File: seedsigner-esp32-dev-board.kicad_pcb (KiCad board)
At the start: 2 copper layers, 73.7 x 86.4 mm, 4 parts, among them J1 Conn_01x05, U1 ESP32-S2-SAOLA-1M, U2 OV_CAMERA, U3 RASPBERRY_PI_3_MODEL_B+

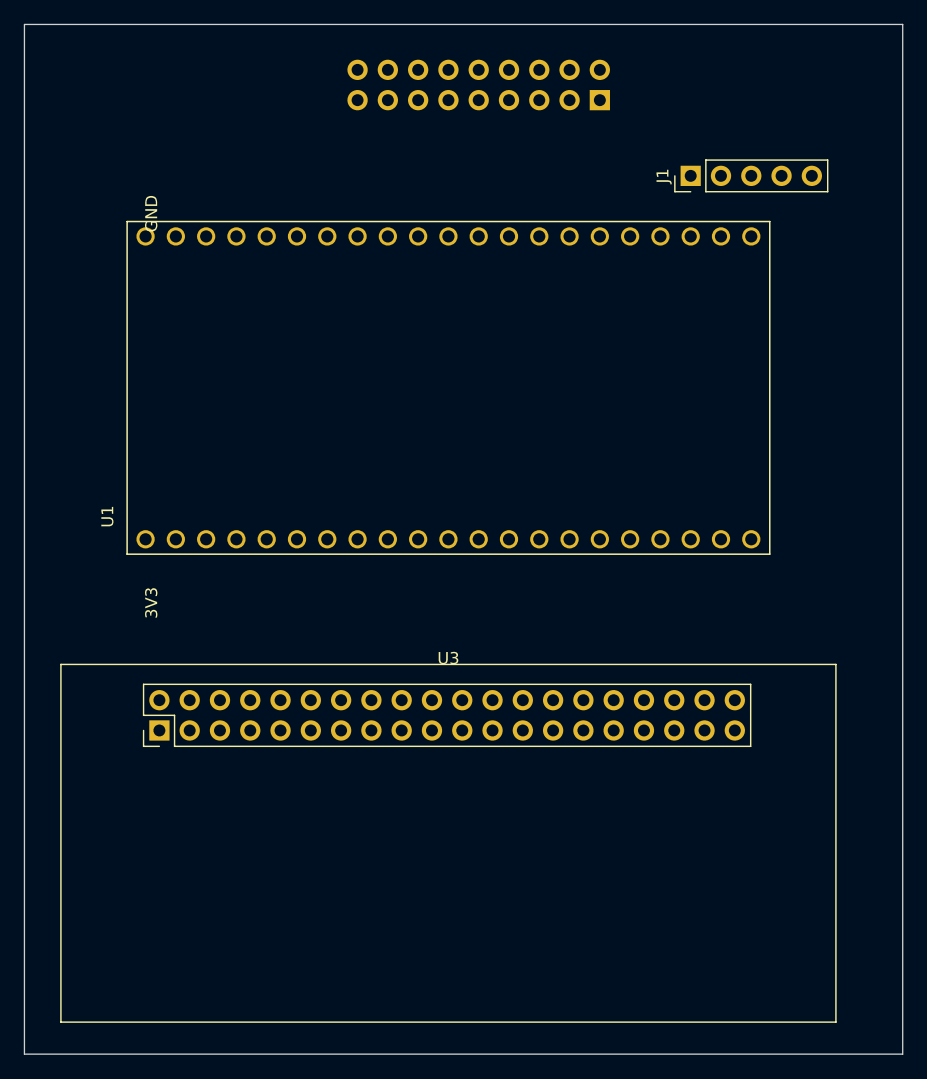
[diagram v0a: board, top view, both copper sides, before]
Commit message: add symbol libraries
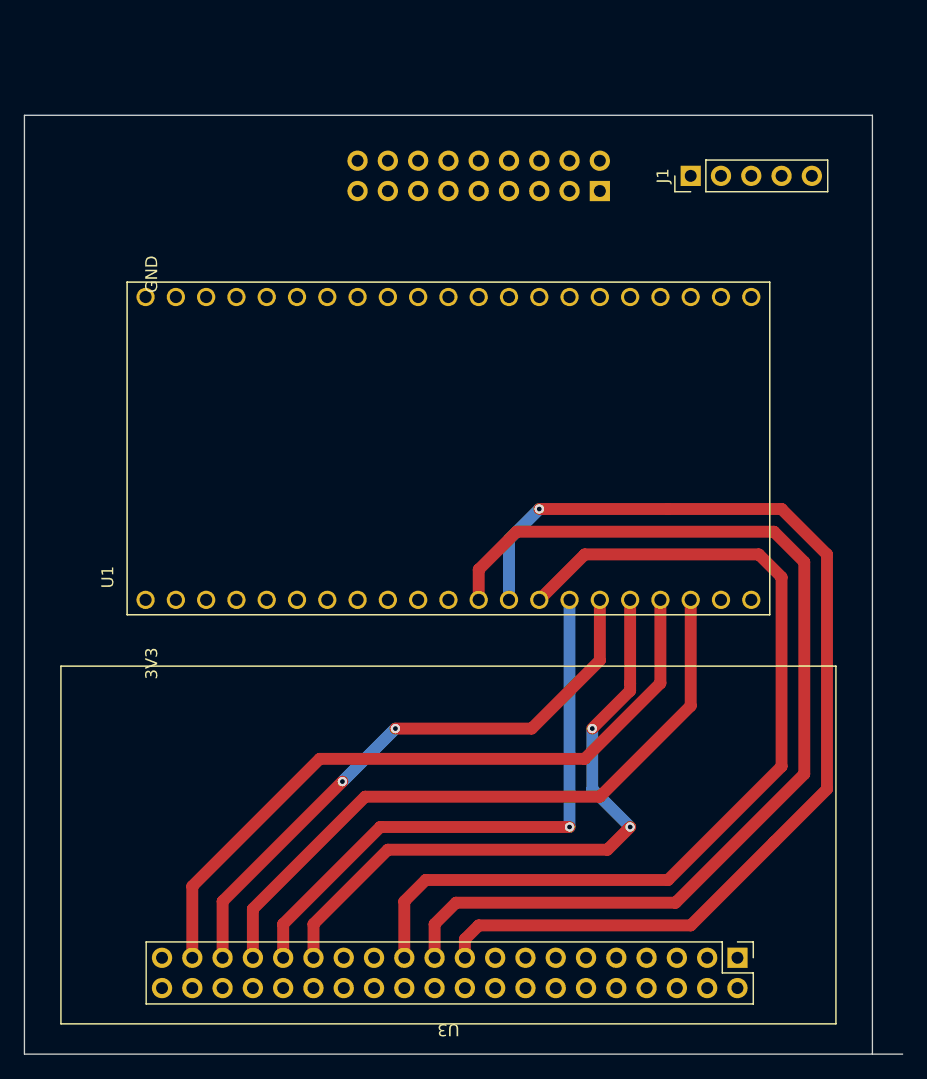
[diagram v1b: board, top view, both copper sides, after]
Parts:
- moved U3 30.1 mm to (162.6, 124.5), turned to 180 degrees
- moved U2 7.62 mm to (165.1, 53.3)
- moved U1 5.08 mm to (162.6, 76.2)
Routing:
- net /SPI_MOSI: track 0.00 -> 91.2 mm, vias 0 -> 1
- net /SPI_CS: track 0.00 -> 89.0 mm
- net /SPI_SCLK: track 0.00 -> 79.6 mm
- net /JOYSTICK_RIGHT: track 0.00 -> 59.3 mm
- net /JOYSTICK_PRESS: track 0.00 -> 56.8 mm
- net /JOYSTICK_LEFT: track 0.00 -> 54.4 mm, vias 0 -> 2
- net /JOYSTICK_DOWN: track 0.00 -> 49.8 mm, vias 0 -> 2
- net /JOYSTICK_UP: track 0.00 -> 49.3 mm, vias 0 -> 1
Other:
- board size 73.7 x 86.4 mm -> 73.7 x 78.7 mm

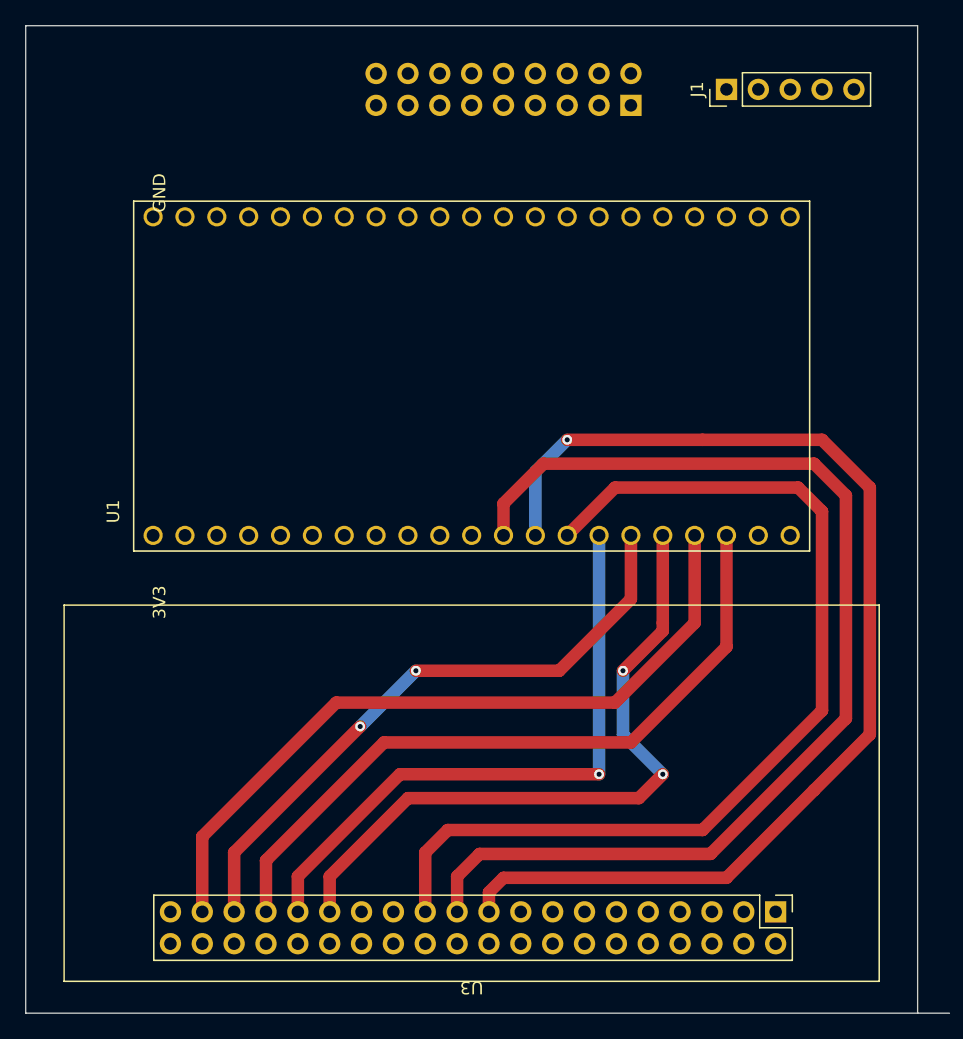
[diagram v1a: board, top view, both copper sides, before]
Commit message: update readme with links, add 3.3v to display and cap
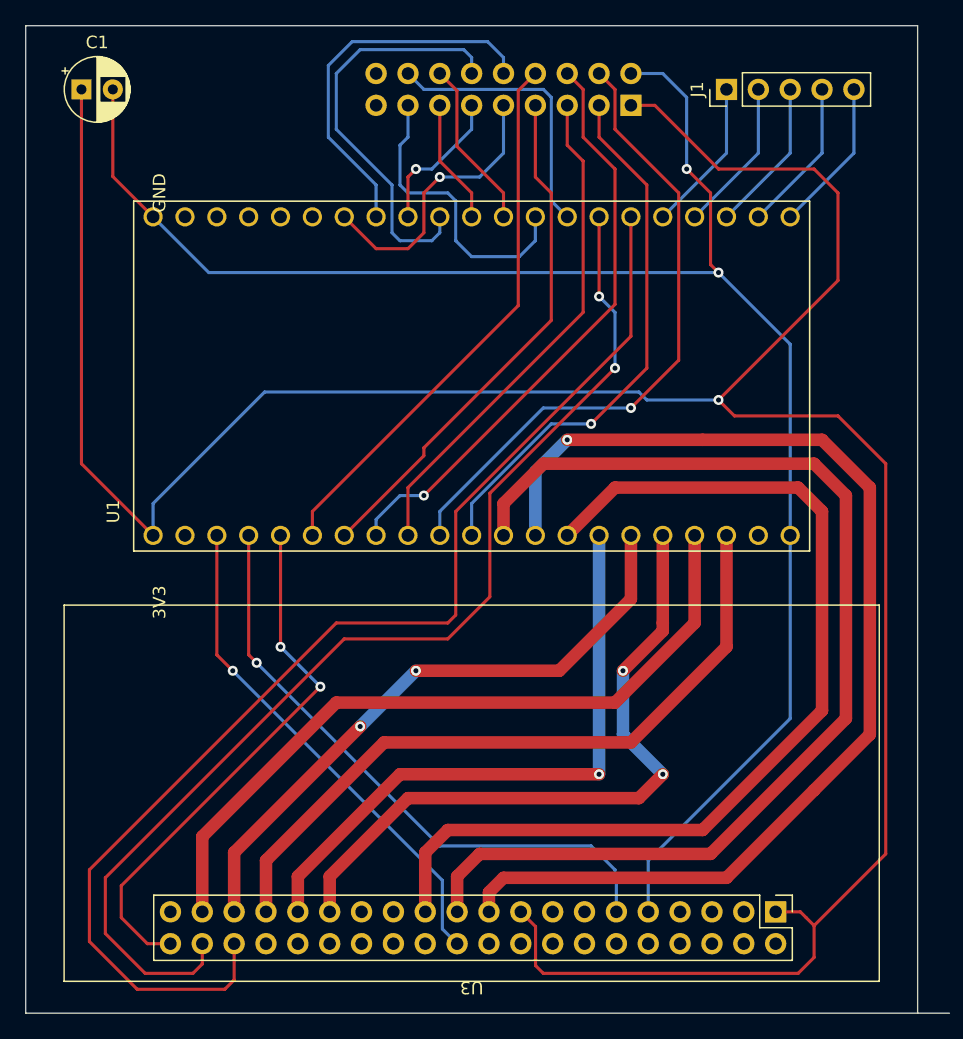
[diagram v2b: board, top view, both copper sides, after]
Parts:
- added C1: C_Polarized, Capacitor_THT:CP_Radial_D5.0mm_P2.50mm, F.Cu at (131.4, 53.3)
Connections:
- U3 pad 1: Net-(U3-Pad1) -> +3.3V
- U3 pad 17: Net-(U3-Pad1) -> +3.3V
- U3 pad 36: unconnected-(U3-Pad36) -> /KEY3
- U3 pad 38: unconnected-(U3-Pad38) -> /KEY2
- U3 pad 40: unconnected-(U3-Pad40) -> /KEY1
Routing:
- net +3.3V: track 0.00 -> 217.8 mm, vias 0 -> 1
- net GND: track 0.00 -> 136.7 mm, vias 0 -> 2
- net /KEY3: track 0.00 -> 97.2 mm
- net /KEY2: track 0.00 -> 90.3 mm, vias 0 -> 2
- net /SDA: track 0.00 -> 51.4 mm, vias 0 -> 1
- net /RST: track 0.00 -> 49.2 mm, vias 0 -> 1
- net /HREF: track 0.00 -> 47.4 mm, vias 0 -> 1
- net /XCLK: track 0.00 -> 44.2 mm
- net /SCL: track 0.00 -> 43.5 mm, vias 0 -> 1
- net /KEY1: track 0.00 -> 43.2 mm, vias 0 -> 2
- net /PCLK: track 0.00 -> 41.7 mm
- net /VSYNC: track 0.00 -> 40.6 mm
- net /DC: track 0.00 -> 40.5 mm, vias 0 -> 1
- net /D6: track 0.00 -> 33.3 mm
- net /D8: track 0.00 -> 30.2 mm
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
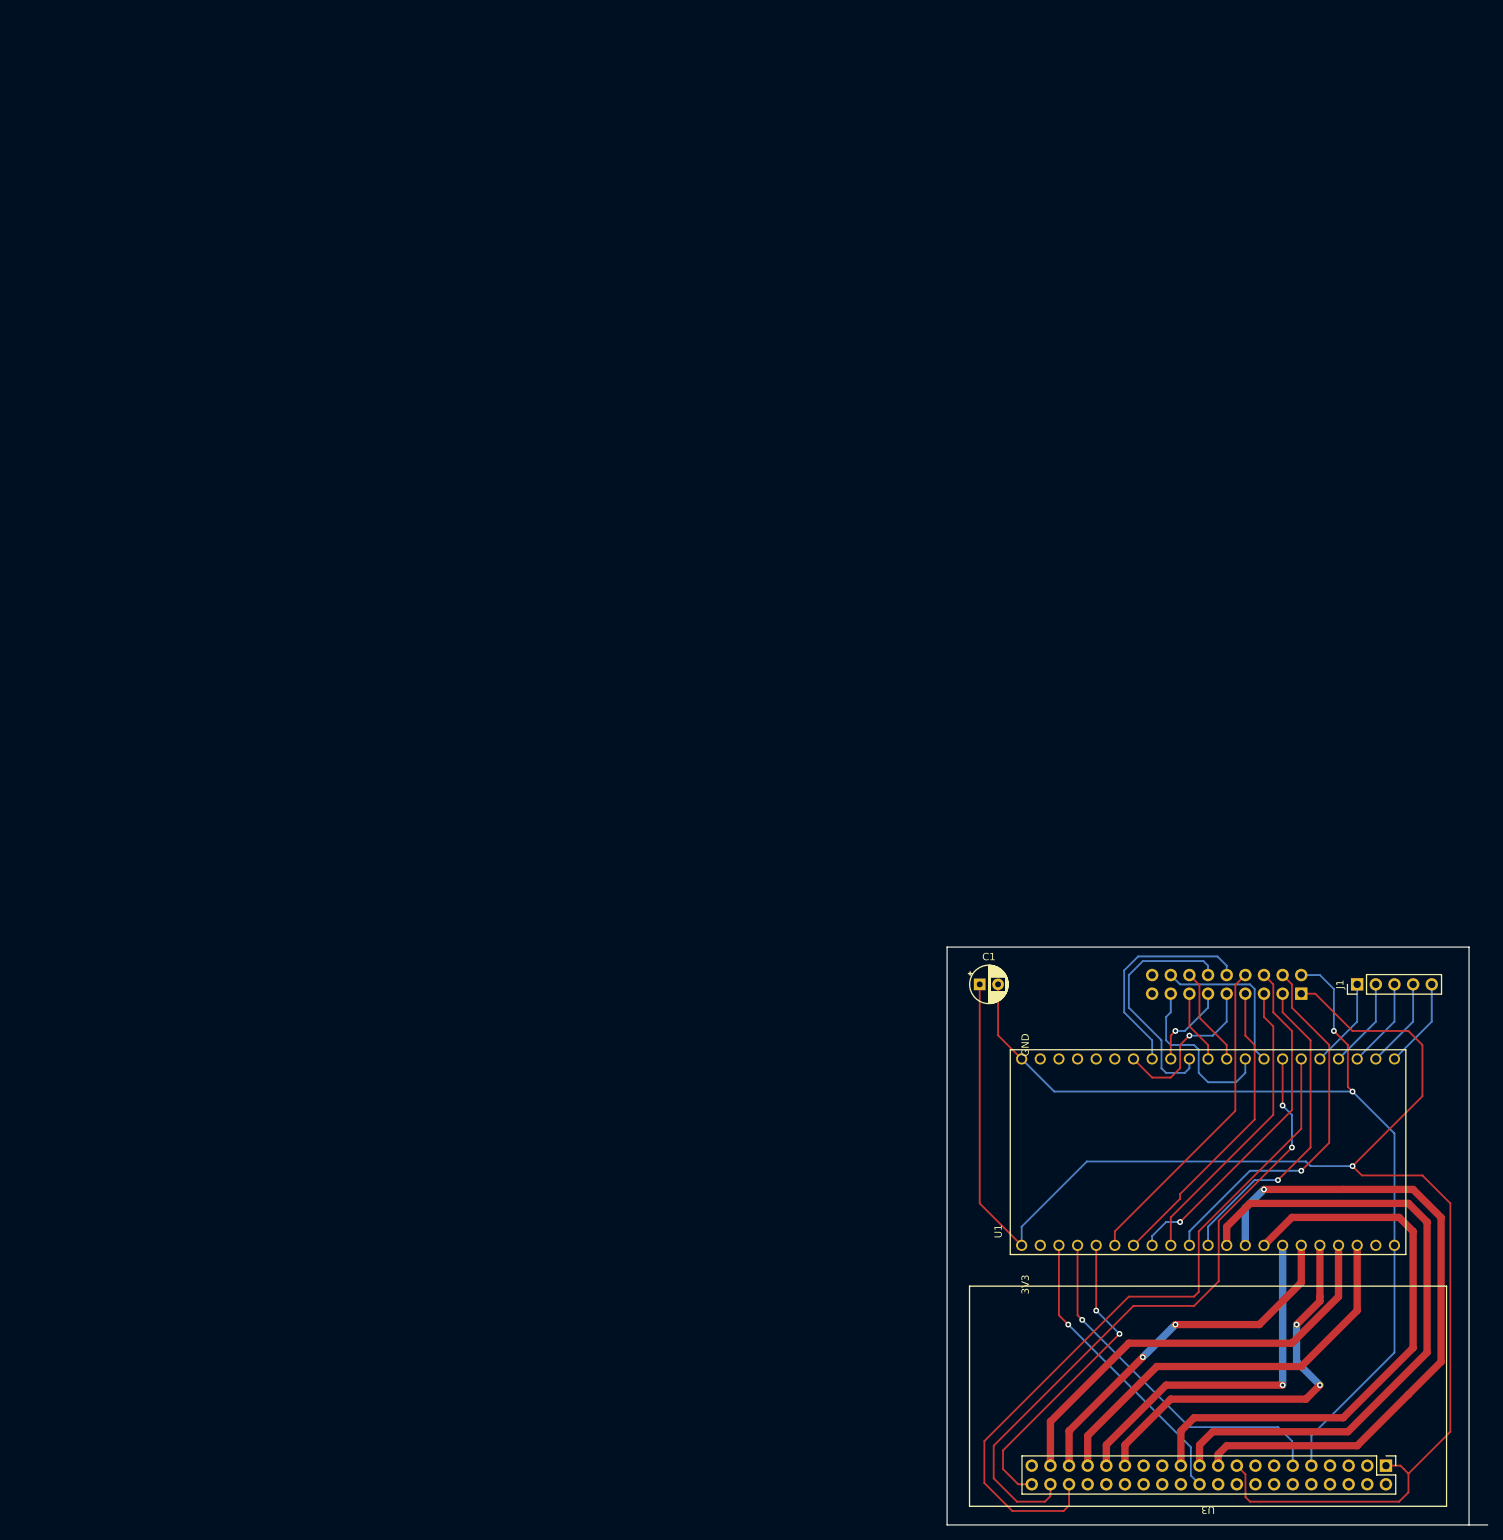
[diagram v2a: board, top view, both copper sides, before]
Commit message: rewire all the pins to make routing cleaner
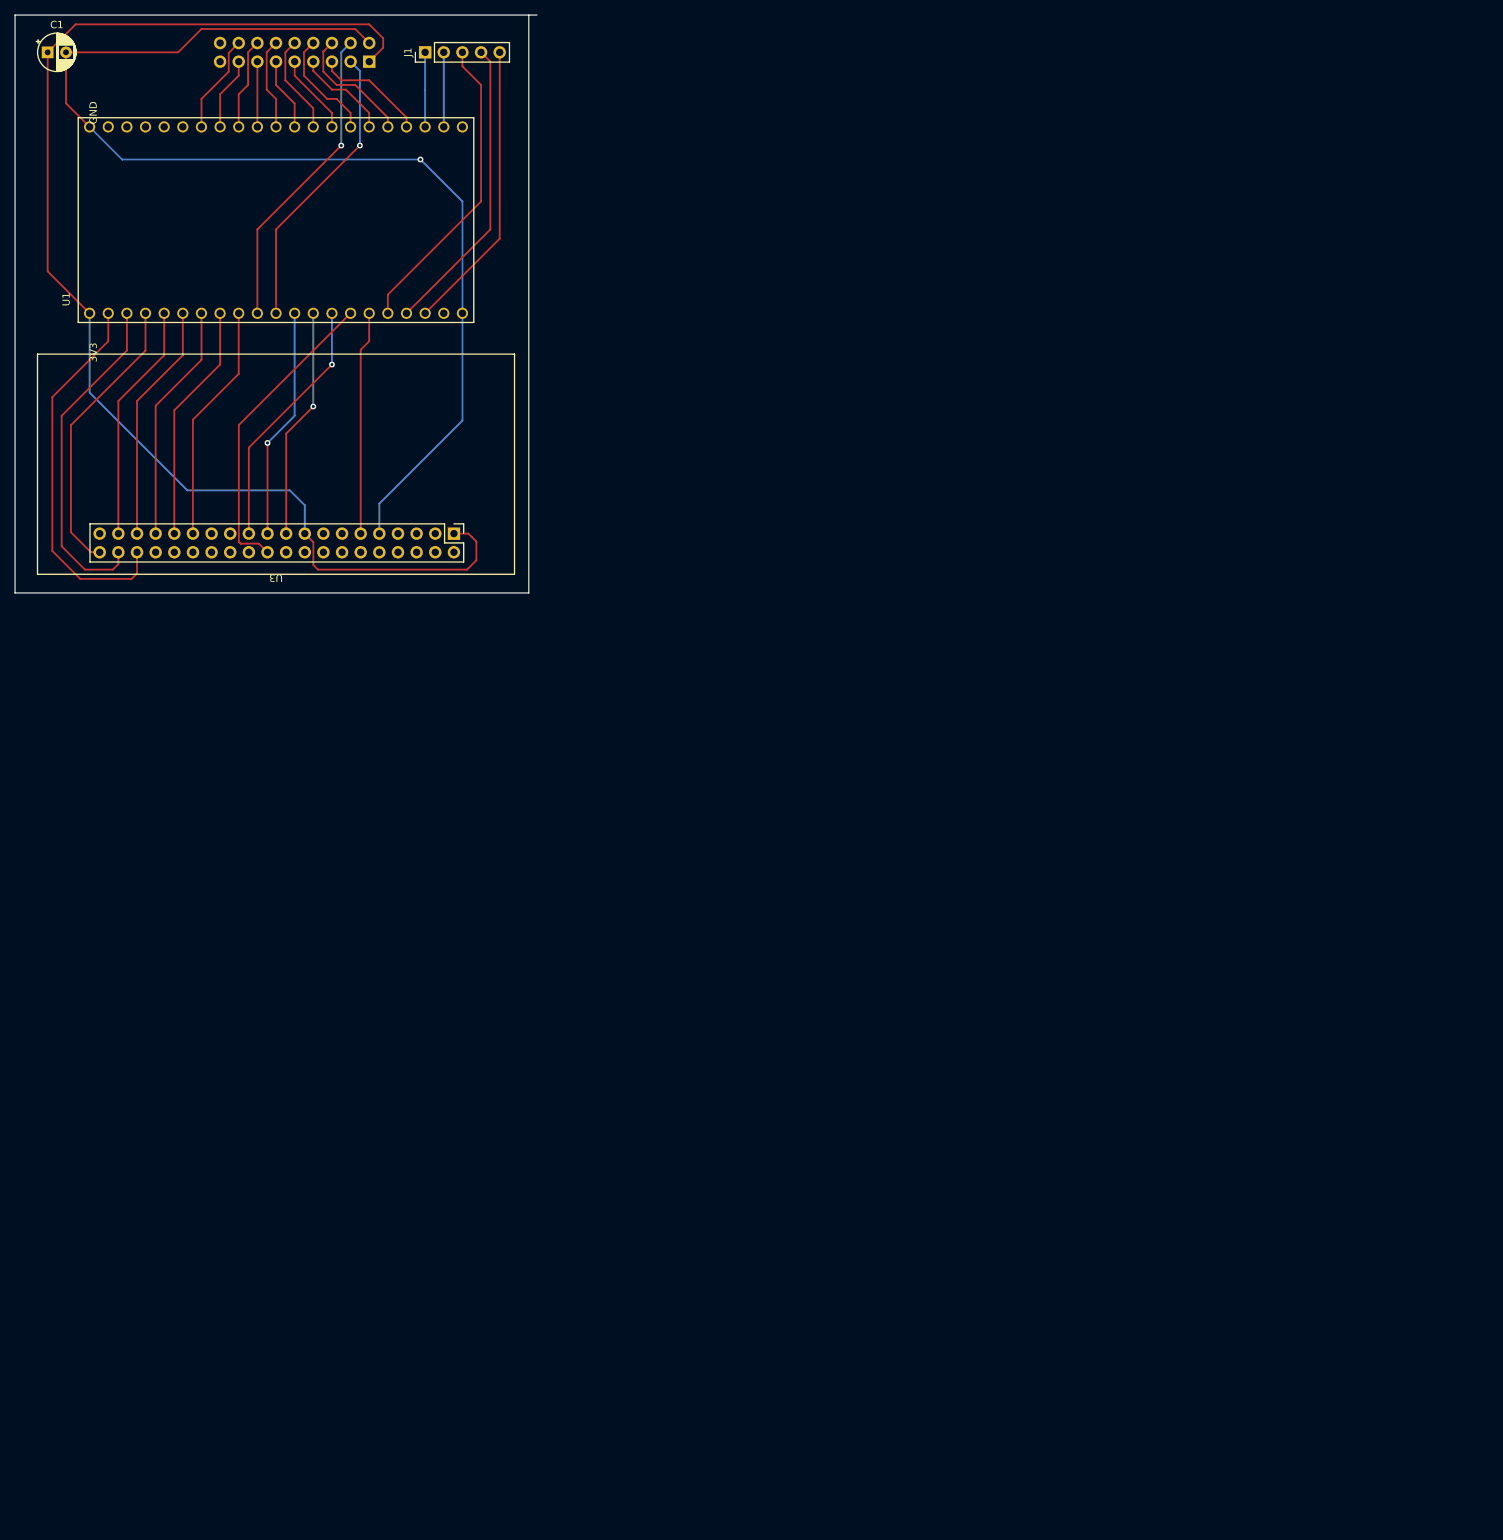
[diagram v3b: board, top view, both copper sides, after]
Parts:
- moved C1 179.6 mm to (4.45, -73.7)
- moved J1 179.6 mm to (55.9, -73.7)
- moved U1 179.6 mm to (35.6, -50.8)
- moved U2 179.6 mm to (38.1, -73.7)
- moved U3 179.6 mm to (35.6, -2.54)
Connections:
- J1 pad 1: Net-(J1-Pad1) -> /XTRA1
- J1 pad 2: Net-(J1-Pad2) -> /XTRA2
- J1 pad 3: Net-(J1-Pad3) -> /XTRA3
- J1 pad 4: Net-(J1-Pad4) -> /XTRA4
- J1 pad 5: Net-(J1-Pad5) -> /XTRA5
- U1 pad 0: unconnected-(U1-Pad0) -> /KEY3
- U1 pad 1: /DC -> /KEY2
- U1 pad 13: /JOYSTICK_UP -> /DC
- U1 pad 14: /JOYSTICK_DOWN -> /RST
- U1 pad 15: /JOYSTICK_LEFT -> /XTRA3
- U1 pad 16: /JOYSTICK_RIGHT -> /XTRA4
- U1 pad 17: /JOYSTICK_PRESS -> /XTRA5
- U1 pad 18: Net-(J1-Pad5) -> unconnected-(U1-Pad18)
- U1 pad 19: Net-(J1-Pad4) -> /XTRA2
- U1 pad 2: /RST -> /KEY1
- U1 pad 20: Net-(J1-Pad3) -> /XTRA1
- U1 pad 21: Net-(J1-Pad2) -> /VSYNC
- U1 pad 26: Net-(J1-Pad1) -> /HREF
- U1 pad 3: /KEY1 -> /JOYSTICK_RIGHT
- U1 pad 33: /KEY3 -> /PCLK
- U1 pad 34: /KEY2 -> /XCLK
- U1 pad 35: /D2 -> /D9
- U1 pad 36: /D3 -> /D8
- U1 pad 37: /D4 -> /D7
- U1 pad 38: /D5 -> /D6
- U1 pad 39: /D6 -> /D5
- U1 pad 4: /XCLK -> /JOYSTICK_DOWN
- U1 pad 40: /D7 -> /D4
- U1 pad 41: /D8 -> /D3
- U1 pad 42: /D9 -> /D2
- U1 pad 5: /PCLK -> /JOYSTICK_PRESS
- U1 pad 6: /HREF -> /JOYSTICK_UP
- U1 pad 7: /VSYNC -> /JOYSTICK_LEFT
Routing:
- net /SPI_MOSI: track 91.2 -> 31.6 mm
- net /SPI_CS: track 89.0 -> 31.6 mm, vias 0 -> 1
- net /KEY3: track 97.2 -> 51.9 mm
- net /SPI_SCLK: track 79.6 -> 34.7 mm, vias 0 -> 1
- net /KEY2: track 90.3 -> 46.4 mm, vias 2 -> 0
- net +3.3V: track 217.8 -> 174.1 mm, vias 1 -> 0
- net /XTRA3: track 0.00 -> 41.9 mm
- net /XTRA4: track 0.00 -> 40.8 mm
- net /XTRA5: track 0.00 -> 39.8 mm
- net /HREF: track 47.4 -> 17.0 mm, vias 1 -> 0
- net /XCLK: track 44.2 -> 15.3 mm
- net /PCLK: track 41.7 -> 13.2 mm
- net /JOYSTICK_RIGHT: track 59.3 -> 32.6 mm
- net /VSYNC: track 40.6 -> 15.3 mm
- net /JOYSTICK_PRESS: track 56.8 -> 32.6 mm
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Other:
- board size 73.7 x 78.7 mm -> 71.1 x 78.7 mm
